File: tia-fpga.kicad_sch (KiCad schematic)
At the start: 24 parts, among them J1 Tang Nano 9K - mates J5, J2 TIA pins 1-20, J3 TIA pins 21-40, J4 Tang Nano 9K - mates J6, U1 74AHCT125, U2 74LVC245A, U3 74LVC541A, U4 74LVC541A, U5 74LVC1G32

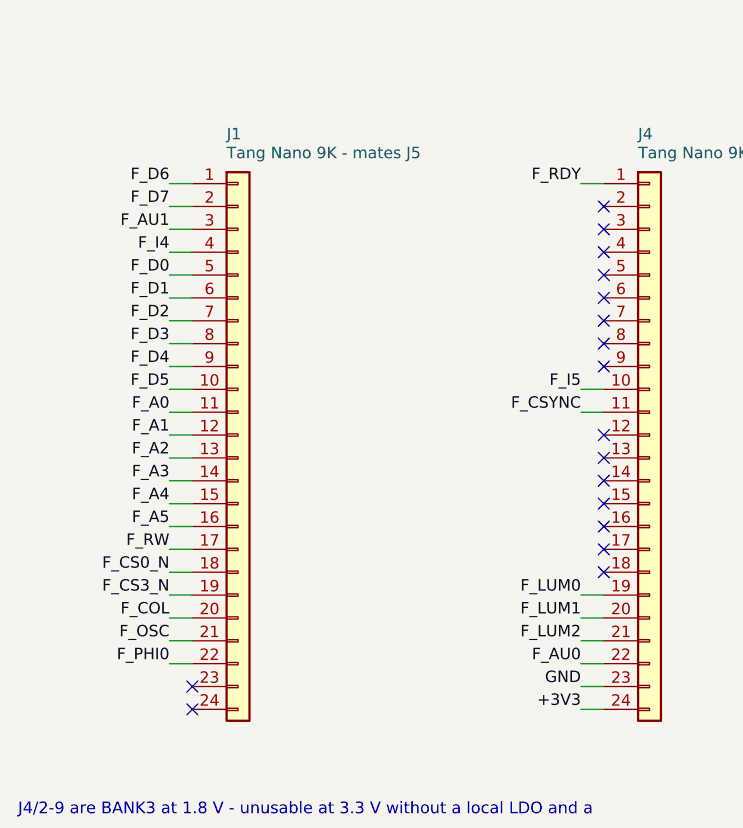
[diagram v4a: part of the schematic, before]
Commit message: Solve the pin assignment and reorder the buffers; drop the mounting holes
The buses crossed the board because the FPGA signals were assigned to
header positions in listing order. But which GPIO carries which signal is
free - the Tang Nano's header-to-package map is fixed, nothing says F_D0
has to sit on header pin 5. So it is now solved rather than listed:
Hungarian assignment over the 29 usable positions, minimising the
distance from each FPGA pin to the TIA pin it serves.

Summed |x_header - x_TIA| goes from 737 mm to 127 mm, with several
signals landing at exactly the same x as their target. The buffers are
then ordered by the centroid of what each carries: U1, U4, U3, U2.

Together:

  segments  758 -> 601
  vias       47 -> 31
  copper   2.19 -> 1.68 m

Mounting holes dropped. They were only ever going to hold the board to
something that does not exist inside a 2600 - it hangs from its own pins
in the TIA socket - and they had pushed the outline out to 76 x 36 mm.
Back to 70 x 32.

Silkscreen references moved beside the passives rather than above them;
in a 5 mm margin, above means into the board edge. That took the
silkscreen violations from 11 to 1.

Routing needed 0.18 mm track on top of the 0.13 mm clearance to close.
Worth recording how brittle this is: moving U5 by half a millimetre to
clear a courtyard warning cost two unrouted connections and a worse
score, because Freerouting is deterministic per input and any change
reshuffles everything. U5 went back where it was.

DRC: 0 clearance, 0 unconnected, 0 shorts. Two notes remain, both checked
by hand - one silk mark over copper, and the U5/J1 courtyard overlap
where the copper actually clears by 1.24 mm.

fpga/tia_fpga.cst carries the solved assignment and says not to reshuffle
it casually, since the layout depends on it.

Co-Authored-By: Claude Opus 5 <noreply@anthropic.com>
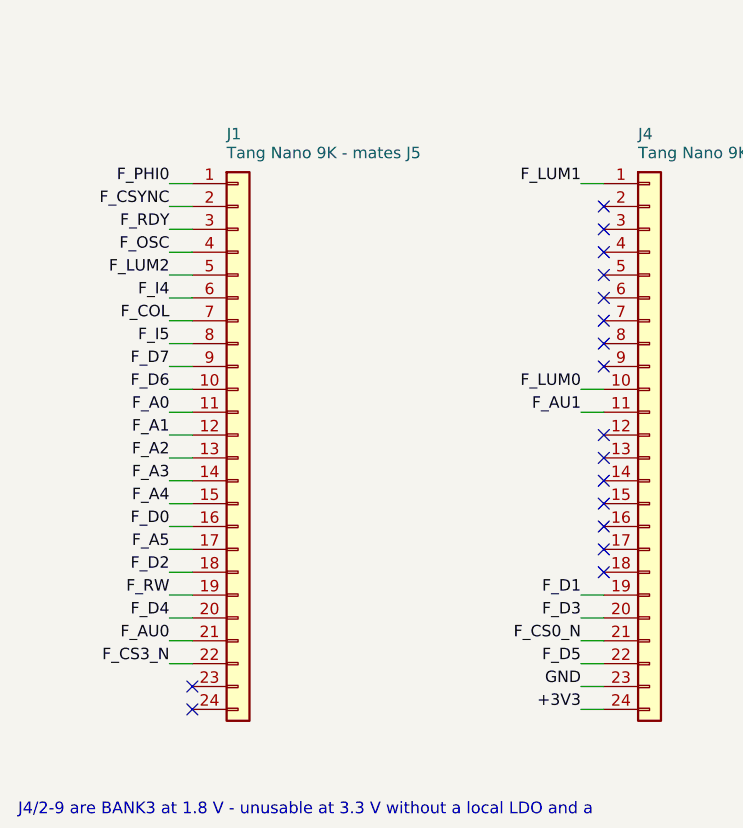
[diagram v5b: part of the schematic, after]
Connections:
- net F_A5: now also J1.17 (Pin_17); no longer J1.16 (Pin_16)
- net F_AU0: now also J1.21 (Pin_21); no longer J4.22 (Pin_22)
- net F_AU1: now also J4.11 (Pin_11); no longer J1.3 (Pin_3)
- net F_COL: now also J1.7 (Pin_7); no longer J1.20 (Pin_20)
- net F_CS0_N: now also J4.21 (Pin_21); no longer J1.18 (Pin_18)
- net F_CS3_N: now also J1.22 (Pin_22); no longer J1.19 (Pin_19)
- net F_CSYNC: now also J1.2 (Pin_2); no longer J4.11 (Pin_11)
- net F_D0: now also J1.16 (Pin_16); no longer J1.5 (Pin_5)
- net F_D1: now also J4.19 (Pin_19); no longer J1.6 (Pin_6)
- net F_D2: now also J1.18 (Pin_18); no longer J1.7 (Pin_7)
- net F_D3: now also J4.20 (Pin_20); no longer J1.8 (Pin_8)
- net F_D4: now also J1.20 (Pin_20); no longer J1.9 (Pin_9)
- net F_D5: now also J4.22 (Pin_22); no longer J1.10 (Pin_10)
- net F_D6: now also J1.10 (Pin_10); no longer J1.1 (Pin_1)
- net F_D7: now also J1.9 (Pin_9); no longer J1.2 (Pin_2)
- net F_I4: now also J1.6 (Pin_6); no longer J1.4 (Pin_4)
- net F_I5: now also J1.8 (Pin_8); no longer J4.10 (Pin_10)
- net F_LUM0: now also J4.10 (Pin_10); no longer J4.19 (Pin_19)
- net F_LUM1: now also J4.1 (Pin_1); no longer J4.20 (Pin_20)
- net F_LUM2: now also J1.5 (Pin_5); no longer J4.21 (Pin_21)
- net F_OSC: now also J1.4 (Pin_4); no longer J1.21 (Pin_21)
- net F_PHI0: now also J1.1 (Pin_1); no longer J1.22 (Pin_22)
- net F_RDY: now also J1.3 (Pin_3); no longer J4.1 (Pin_1)
- net F_RW: now also J1.19 (Pin_19); no longer J1.17 (Pin_17)
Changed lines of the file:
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@@
 		(instances
 			(project "tia-fpga"
-				(path "/2e306981-9160-43af-a437-b150d51b2219"
+				(path "/b310daf3-ae03-4c4a-85d5-0b0546462b61"
 					(reference "J1")
 					(unit 1)
@@
 		)
 	)
-	(label "F_D6"
+	(label "F_PHI0"
 		(at 36.83 72.39 0)
 		(effects
@@
 		)
 	)
-	(label "F_D7"
+	(label "F_CSYNC"
 		(at 36.83 74.93 0)
 		(effects
@@
 		)
 	)
-	(label "F_AU1"
+	(label "F_RDY"
 		(at 36.83 77.47 0)
 		(effects
@@
 		)
 	)
-	(label "F_I4"
+	(label "F_OSC"
 		(at 36.83 80.01 0)
 		(effects
@@
 		)
 	)
-	(label "F_D0"
+	(label "F_LUM2"
 		(at 36.83 82.55 0)
 		(effects
@@
 		)
 	)
-	(label "F_D1"
+	(label "F_I4"
 		(at 36.83 85.09 0)
 		(effects
@@
 		)
 	)
-	(label "F_D2"
+	(label "F_COL"
 		(at 36.83 87.63 0)
 		(effects
@@
 		)
 	)
-	(label "F_D3"
+	(label "F_I5"
 		(at 36.83 90.17 0)
 		(effects
@@
 		)
 	)
-	(label "F_D4"
+	(label "F_D7"
 		(at 36.83 92.71 0)
 		(effects
@@
 		)
 	)
-	(label "F_D5"
+	(label "F_D6"
 		(at 36.83 95.25 0)
 		(effects
@@
 		)
 	)
-	(label "F_A5"
+	(label "F_D0"
 		(at 36.83 110.49 0)
 		(effects
@@
 		)
 	)
-	(label "F_RW"
+	(label "F_A5"
 		(at 36.83 113.03 0)
 		(effects
@@
 		)
 	)
-	(label "F_CS0_N"
+	(label "F_D2"
 		(at 36.83 115.57 0)
 		(effects
@@
 		)
 	)
-	(label "F_CS3_N"
+	(label "F_RW"
 		(at 36.83 118.11 0)
 		(effects
@@
 		)
 	)
-	(label "F_COL"
+	(label "F_D4"
 		(at 36.83 120.65 0)
 		(effects
@@
 		)
 	)
-	(label "F_OSC"
+	(label "F_AU0"
 		(at 36.83 123.19 0)
 		(effects
@@
 		)
 	)
-	(label "F_PHI0"
+	(label "F_CS3_N"
 		(at 36.83 125.73 0)
 		(effects
@@
 		(instances
 			(project "tia-fpga"
-				(path "/2e306981-9160-43af-a437-b150d51b2219"
+				(path "/b310daf3-ae03-4c4a-85d5-0b0546462b61"
 					(reference "J4")
 					(unit 1)
@@
 		)
 	)
-	(label "F_RDY"
+	(label "F_LUM1"
 		(at 82.55 72.39 0)
 		(effects
@@
 		)
 	)
-	(label "F_I5"
+	(label "F_LUM0"
 		(at 82.55 95.25 0)
 		(effects
@@
 		)
 	)
-	(label "F_CSYNC"
+	(label "F_AU1"
 		(at 82.55 97.79 0)
 		(effects
@@
 		)
 	)
-	(label "F_LUM0"
+	(label "F_D1"
 		(at 82.55 118.11 0)
 		(effects
@@
 		)
 	)
-	(label "F_LUM1"
+	(label "F_D3"
 		(at 82.55 120.65 0)
 		(effects
@@
 		)
 	)
-	(label "F_LUM2"
+	(label "F_CS0_N"
 		(at 82.55 123.19 0)
 		(effects
@@
 		)
 	)
-	(label "F_AU0"
+	(label "F_D5"
 		(at 82.55 125.73 0)
 		(effects
@@
 		(instances
 			(project "tia-fpga"
-				(path "/2e306981-9160-43af-a437-b150d51b2219"
+				(path "/b310daf3-ae03-4c4a-85d5-0b0546462b61"
 					(reference "U1")
 					(unit 1)
@@
 		(instances
 			(project "tia-fpga"
-				(path "/2e306981-9160-43af-a437-b150d51b2219"
+				(path "/b310daf3-ae03-4c4a-85d5-0b0546462b61"
 					(reference "U1")
 					(unit 2)
@@
 		(instances
 			(project "tia-fpga"
-				(path "/2e306981-9160-43af-a437-b150d51b2219"
+				(path "/b310daf3-ae03-4c4a-85d5-0b0546462b61"
 					(reference "U1")
 					(unit 3)
@@
 		(instances
 			(project "tia-fpga"
-				(path "/2e306981-9160-43af-a437-b150d51b2219"
+				(path "/b310daf3-ae03-4c4a-85d5-0b0546462b61"
 					(reference "U1")
 					(unit 4)
@@
 		(instances
 			(project "tia-fpga"
-				(path "/2e306981-9160-43af-a437-b150d51b2219"
+				(path "/b310daf3-ae03-4c4a-85d5-0b0546462b61"
 					(reference "U1")
 					(unit 5)
@@
 		(instances
 			(project "tia-fpga"
-				(path "/2e306981-9160-43af-a437-b150d51b2219"
+				(path "/b310daf3-ae03-4c4a-85d5-0b0546462b61"
 					(reference "U2")
 					(unit 1)
@@
 		(instances
 			(project "tia-fpga"
-				(path "/2e306981-9160-43af-a437-b150d51b2219"
+				(path "/b310daf3-ae03-4c4a-85d5-0b0546462b61"
 					(reference "U5")
 					(unit 1)
@@
 		(instances
 			(project "tia-fpga"
-				(path "/2e306981-9160-43af-a437-b150d51b2219"
+				(path "/b310daf3-ae03-4c4a-85d5-0b0546462b61"
 					(reference "U3")
 					(unit 1)
@@
 		(instances
 			(project "tia-fpga"
-				(path "/2e306981-9160-43af-a437-b150d51b2219"
+				(path "/b310daf3-ae03-4c4a-85d5-0b0546462b61"
 					(reference "U4")
 					(unit 1)
@@
 		(instances
 			(project "tia-fpga"
-				(path "/2e306981-9160-43af-a437-b150d51b2219"
+				(path "/b310daf3-ae03-4c4a-85d5-0b0546462b61"
 					(reference "J2")
 					(unit 1)
@@
 		(instances
 			(project "tia-fpga"
-				(path "/2e306981-9160-43af-a437-b150d51b2219"
+				(path "/b310daf3-ae03-4c4a-85d5-0b0546462b61"
 					(reference "J3")
 					(unit 1)
@@
 		(instances
 			(project "tia-fpga"
-				(path "/2e306981-9160-43af-a437-b150d51b2219"
+				(path "/b310daf3-ae03-4c4a-85d5-0b0546462b61"
 					(reference "R1")
 					(unit 1)
@@
 		(instances
 			(project "tia-fpga"
-				(path "/2e306981-9160-43af-a437-b150d51b2219"
+				(path "/b310daf3-ae03-4c4a-85d5-0b0546462b61"
 					(reference "R2")
 					(unit 1)
@@
 		(instances
 			(project "tia-fpga"
-				(path "/2e306981-9160-43af-a437-b150d51b2219"
+				(path "/b310daf3-ae03-4c4a-85d5-0b0546462b61"
 					(reference "R3")
 					(unit 1)
@@
 		(instances
 			(project "tia-fpga"
-				(path "/2e306981-9160-43af-a437-b150d51b2219"
+				(path "/b310daf3-ae03-4c4a-85d5-0b0546462b61"
 					(reference "R4")
 					(unit 1)
@@
 		(instances
 			(project "tia-fpga"
-				(path "/2e306981-9160-43af-a437-b150d51b2219"
+				(path "/b310daf3-ae03-4c4a-85d5-0b0546462b61"
 					(reference "R5")
 					(unit 1)
@@
 		(instances
 			(project "tia-fpga"
-				(path "/2e306981-9160-43af-a437-b150d51b2219"
+				(path "/b310daf3-ae03-4c4a-85d5-0b0546462b61"
 					(reference "R6")
 					(unit 1)
@@
 		(instances
 			(project "tia-fpga"
-				(path "/2e306981-9160-43af-a437-b150d51b2219"
+				(path "/b310daf3-ae03-4c4a-85d5-0b0546462b61"
 					(reference "R7")
 					(unit 1)
@@
 		(instances
 			(project "tia-fpga"
-				(path "/2e306981-9160-43af-a437-b150d51b2219"
+				(path "/b310daf3-ae03-4c4a-85d5-0b0546462b61"
 					(reference "R8")
 					(unit 1)
@@
 		(instances
 			(project "tia-fpga"
-				(path "/2e306981-9160-43af-a437-b150d51b2219"
+				(path "/b310daf3-ae03-4c4a-85d5-0b0546462b61"
 					(reference "R9")
 					(unit 1)
@@
 		(instances
 			(project "tia-fpga"
-				(path "/2e306981-9160-43af-a437-b150d51b2219"
+				(path "/b310daf3-ae03-4c4a-85d5-0b0546462b61"
 					(reference "C1")
 					(unit 1)
@@
 		(instances
 			(project "tia-fpga"
-				(path "/2e306981-9160-43af-a437-b150d51b2219"
+				(path "/b310daf3-ae03-4c4a-85d5-0b0546462b61"
 					(reference "C2")
 					(unit 1)
@@
 		(instances
 			(project "tia-fpga"
-				(path "/2e306981-9160-43af-a437-b150d51b2219"
+				(path "/b310daf3-ae03-4c4a-85d5-0b0546462b61"
 					(reference "C3")
 					(unit 1)
@@
 		(instances
 			(project "tia-fpga"
-				(path "/2e306981-9160-43af-a437-b150d51b2219"
+				(path "/b310daf3-ae03-4c4a-85d5-0b0546462b61"
 					(reference "C4")
 					(unit 1)
@@
 		(instances
 			(project "tia-fpga"
-				(path "/2e306981-9160-43af-a437-b150d51b2219"
+				(path "/b310daf3-ae03-4c4a-85d5-0b0546462b61"
 					(reference "C5")
 					(unit 1)
@@
 		(instances
 			(project "tia-fpga"
-				(path "/2e306981-9160-43af-a437-b150d51b2219"
+				(path "/b310daf3-ae03-4c4a-85d5-0b0546462b61"
 					(reference "C6")
 					(unit 1)
@@
 		(instances
 			(project "tia-fpga"
-				(path "/2e306981-9160-43af-a437-b150d51b2219"
+				(path "/b310daf3-ae03-4c4a-85d5-0b0546462b61"
 					(reference "#FLG1")
 					(unit 1)
@@
 		(instances
 			(project "tia-fpga"
-				(path "/2e306981-9160-43af-a437-b150d51b2219"
+				(path "/b310daf3-ae03-4c4a-85d5-0b0546462b61"
 					(reference "#FLG2")
 					(unit 1)
@@
 		(instances
 			(project "tia-fpga"
-				(path "/2e306981-9160-43af-a437-b150d51b2219"
+				(path "/b310daf3-ae03-4c4a-85d5-0b0546462b61"
 					(reference "#FLG3")
 					(unit 1)
@@
 		(instances
 			(project "tia-fpga"
-				(path "/2e306981-9160-43af-a437-b150d51b2219"
+				(path "/b310daf3-ae03-4c4a-85d5-0b0546462b61"
 					(reference "#PWR1")
 					(unit 1)
@@
 		(instances
 			(project "tia-fpga"
-				(path "/2e306981-9160-43af-a437-b150d51b2219"
+				(path "/b310daf3-ae03-4c4a-85d5-0b0546462b61"
 					(reference "#PWR2")
 					(unit 1)
@@
 		(instances
 			(project "tia-fpga"
-				(path "/2e306981-9160-43af-a437-b150d51b2219"
+				(path "/b310daf3-ae03-4c4a-85d5-0b0546462b61"
 					(reference "#PWR3")
 					(unit 1)

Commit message: Respin the board as rev B: open-drain pads and BLK
Every TIA video and sound pad is open drain on the die, and the console's
pull-ups and summing network are built around that. Rev B puts SYNC,
LUM0-2, COL, BLK, AUD0 and AUD1 through four 74LVC2G07 (U6-U9, SOT-23-6,
5 V tolerant open-drain outputs) in the top margin above J2, with 100 nF
C7-C10 beside them. Their designators are on the back silkscreen, since
the front has no room left.

BLK (pin 6) is now driven. The original 2600 and the 2600A rev 16 feed it
into the chroma node, which holds the colour burst down during blanking.
The FPGA pin for it comes from reading /CS0 OR /CS3 straight off U5 (net
F_CS_N, the signal that already enables U2) instead of both selects;
tia_board.v ties the core's cs3_n low.

R1-R9 are gone. They copied the console's own video DAC and summing
network, which a board in the TIA socket must not duplicate. C1-C6 moved
to the bottom margin. F_OSC moved to pin 63 (RPLL_T_in, J6/1), so the
colour clock reaches the PLL on its dedicated input and PR1014 is gone.

The FPGA pin assignment was solved again against the pads each net really
reaches (Hungarian assignment, 378 mm summed). Freerouting 2.2.4 routed it
in 557 segments, 29 vias and 1.29 m of copper (rev A: 601, 31, 1.68 m).
One GND connection at C10 was closed by hand, with a via inside the main
pour. ERC 0; DRC 0 violations, 0 unconnected pads. The gerbers, drill
file, PDFs, BOMs and renders are regenerated. The rev A PDFs are removed,
since rev A was never built.

Timing: hblank_next now comes from the horizontal counter's level decodes
(shb_next, rhb_next) instead of the H@2 pulses. That keeps the phase
divider out of the object clock enables. shb_next also carries RSYNC's
countdown: a restart can land on HMOVE's grid, and the decodes alone
would merge a pulse there although HBLANK comes on at that very half
clock. No trace covers the case, so random runs of HMOVE, RSYNC and HMxx
writes checked hblank_next against HBLANK one clock l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
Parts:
- removed R1, R3: 27k, Resistor_SMD:R_0805_2012Metric, symbol Device:R
- removed R2: 56k, Resistor_SMD:R_0805_2012Metric, symbol Device:R
- removed R4: 110k, Resistor_SMD:R_0805_2012Metric, symbol Device:R
- removed R5, R6, R7, R8: 3k3, Resistor_SMD:R_0805_2012Metric, symbol Device:R
- removed R9: 9k1, Resistor_SMD:R_0805_2012Metric, symbol Device:R
- added C10, C7, C8, C9: 100n, Capacitor_SMD:C_0805_2012Metric, symbol Device:C
- added U6, U7, U8, U9: 74LVC2G07, Package_TO_SOT_SMD:SOT-23-6, symbol 74xGxx:74LVC2G07
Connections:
- net +3V3: now also C10.1, C7.1, C8.1, C9.1, U6.5 (VCC), U7.5 (VCC), U8.5 (VCC), U9.5 (VCC)
- net F_A0: now also J1.12 (Pin_12); no longer J1.11 (Pin_11)
- net F_A1: now also J4.11 (Pin_11); no longer J1.12 (Pin_12)
- net F_A5: now also J1.22 (Pin_22); no longer J1.17 (Pin_17)
- net F_AU0: now also J1.16 (Pin_16), U9.3; no longer J1.21 (Pin_21), J2.13 (Pin_13)
- net F_AU1: now also J1.21 (Pin_21), U9.1; no longer J2.12 (Pin_12), J4.11 (Pin_11)
- net F_COL: now also J1.11 (Pin_11), U8.3; no longer J1.7 (Pin_7), J2.9 (Pin_9)
- net F_CS0_N: no longer J4.21 (Pin_21)
- net F_CS3_N: no longer J1.22 (Pin_22)
- net F_CSYNC: now also J1.5 (Pin_5), U6.1; no longer J1.2 (Pin_2), J2.2 (Pin_2)
- net F_D0: now also J4.10 (Pin_10); no longer J1.16 (Pin_16)
- net F_D1: now also J1.18 (Pin_18); no longer J4.19 (Pin_19)
- net F_D2: now also J1.19 (Pin_19); no longer J1.18 (Pin_18)
- net F_D3: now also J4.19 (Pin_19); no longer J4.20 (Pin_20)
- net F_D4: now also J4.20 (Pin_20); no longer J1.20 (Pin_20)
- net F_D5: now also J1.20 (Pin_20); no longer J4.22 (Pin_22)
- net F_D6: now also J4.21 (Pin_21); no longer J1.10 (Pin_10)
- net F_D7: now also J4.22 (Pin_22); no longer J1.9 (Pin_9)
- net F_I5: now also J1.9 (Pin_9); no longer J1.8 (Pin_8)
- net F_LUM0: now also J1.10 (Pin_10), U8.1; no longer J2.8 (Pin_8), J4.10 (Pin_10)
- net F_LUM1: now also J1.4 (Pin_4), U6.3; no longer J2.5 (Pin_5), J4.1 (Pin_1)
- net F_LUM2: now also J1.7 (Pin_7), U7.3; no longer J1.5 (Pin_5), J2.7 (Pin_7)
- net F_OSC: now also J4.1 (Pin_1); no longer J1.4 (Pin_4)
- net F_RW: now also J1.17 (Pin_17); no longer J1.19 (Pin_19)
- net GND: now also C10.2, C7.2, C8.2, C9.2, U6.2 (GND), U7.2 (GND), U8.2 (GND), U9.2 (GND)
- net TIA_BLK: now reaches J2.6 (Pin_6)
- net TIA_BLK: now also U7.6
- net DBUS_OE_N renamed F_CS_N
- net F_CS_N: now also J1.2 (Pin_2)
- new net F_BLK: J1.8 (Pin_8), U7.1
- new net TIA_AU0: J2.13 (Pin_13), U9.4
- new net TIA_AU1: J2.12 (Pin_12), U9.6
- new net TIA_COL: J2.9 (Pin_9), U8.4
- new net TIA_CSYNC: J2.2 (Pin_2), U6.6
- new net TIA_LUM0: J2.8 (Pin_8), U8.6
- new net TIA_LUM1: J2.5 (Pin_5), U6.4
- new net TIA_LUM2: J2.7 (Pin_7), U7.4
- no-connect marks 29 -> 28
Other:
- note added: "1.8 V-powered buffer. Recovering those 8 pins is the way to the paddles."
- note added: "8 are HDMI differential pairs, 3 are power. Rev B uses all 29, with none spare."
- note added: "BLK pulls low through blanking; the 2600 and the 2600A from rev 16 feed it to the colour network."
- note added: "HDMI - not used by this design"
- note added: "On the die SYNC, LUM0-2, COL, BLK and both sound pads only ever pull down,"
- note added: "Pins 37-40 (paddles) and pin 10 (DEL, the colour trim) are left open:"
- note added: "Rev B - digital interface with open-drain video and sound pads. The paddles do not fit the pin budget."
- note added: "The FPGA reads the same net, F_CS_N, which frees the pin BLK uses."
- note added: "The Tang Nano's HDMI pins are dedicated differential pairs"
- note added: "U5 /OE = /CS0 OR /CS3: the 245 drives the bus only while the TIA is selected."
- note added: "VIDEO AND SOUND PADS - U6-U9, 74LVC2G07: open drain, 5 V tolerant"
- note added: "no FPGA pin is left for the paddles, and DEL has no use here."
- note added: "none yet."
- note added: "outside the 29-pin budget. A TMDS encoder in the FPGA could"
- note added: "send colour out through them at no pin cost; the RTL has"
- note added: "so here the console's own pull-ups set every level, as they do for the TIA."
- note removed: "1.8 V-powered buffer. Recovering those 8 pins is the rev B fix."
- note removed: "4:2:1 luma weighting, plus R9 for chroma. Do NOT populate when the board"
- note removed: "8 are HDMI differential pairs, 3 are power. Rev A uses all 29, with none spare."
- note removed: "COLOUR VIDEO - via the Tang Nano's HDMI connector"
- note removed: "Pin 9 (COL, chroma) and pins 37-40 (paddles) left open:"
- note removed: "Rev A - digital interface only. Chroma and paddles do not fit the pin budget; see the notes."
- note removed: "TMDS encoder drives the HDMI pins, which are dedicated"
- note removed: "The 7-bit colour value never leaves the FPGA: an internal"
- note removed: "U5 /OE = /CS0 OR /CS3. The 245 drives the bus only while the TIA is"
- note removed: "VIDEO OUTPUT - CX-2600A resistor network (STANDALONE USE ONLY)"
- note removed: "differential pairs on the module and were never part of"
- note removed: "goes into a real 2600: the console already has this network, and a second"
- note removed: "no FPGA pin is left for them on a Tang Nano 9K. See README."
- note removed: "one in parallel would shift every level. Drive the socket pins and stop."
- note removed: "selected, so it never fights the ROM or the RIOT on a CPU read."
- note removed: "the 29-pin GPIO budget. Colour costs zero header pins."
